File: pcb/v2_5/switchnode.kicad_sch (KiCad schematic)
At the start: 11 parts, among them Q2 IRLML6402, Q9 2SC1623 300-400

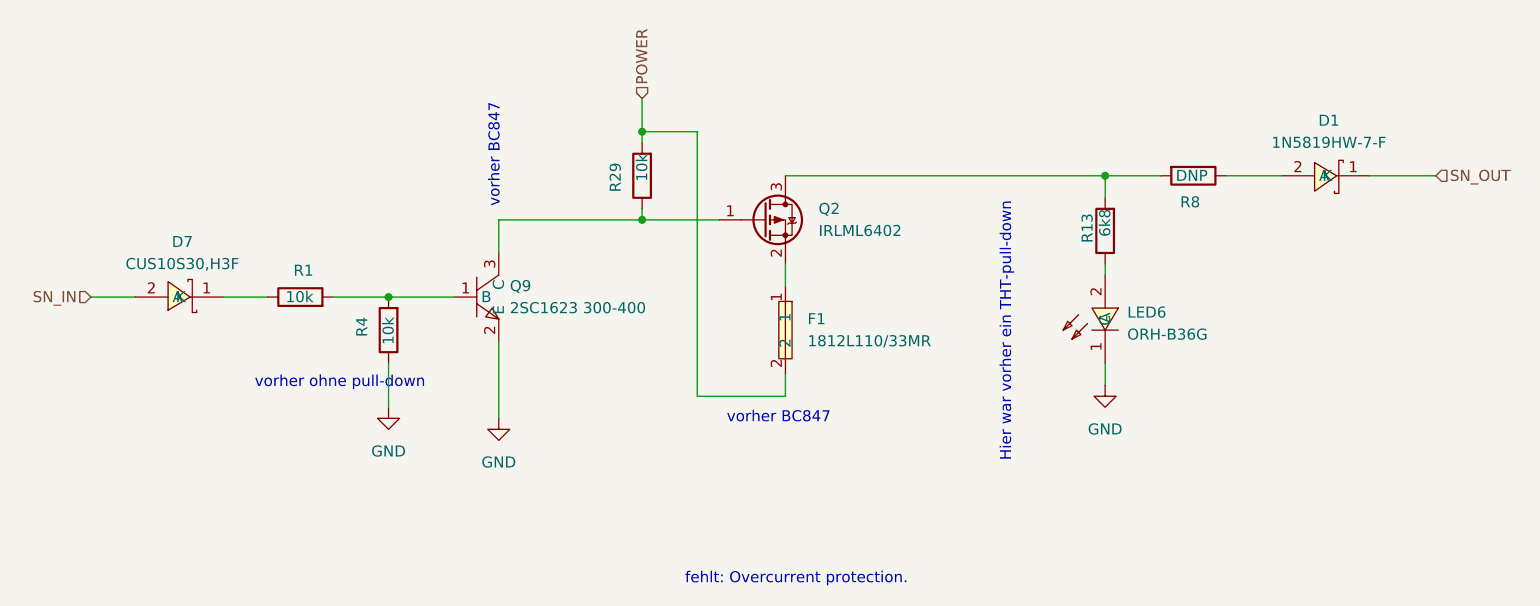
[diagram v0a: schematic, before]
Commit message: added some diodes, fuses etc
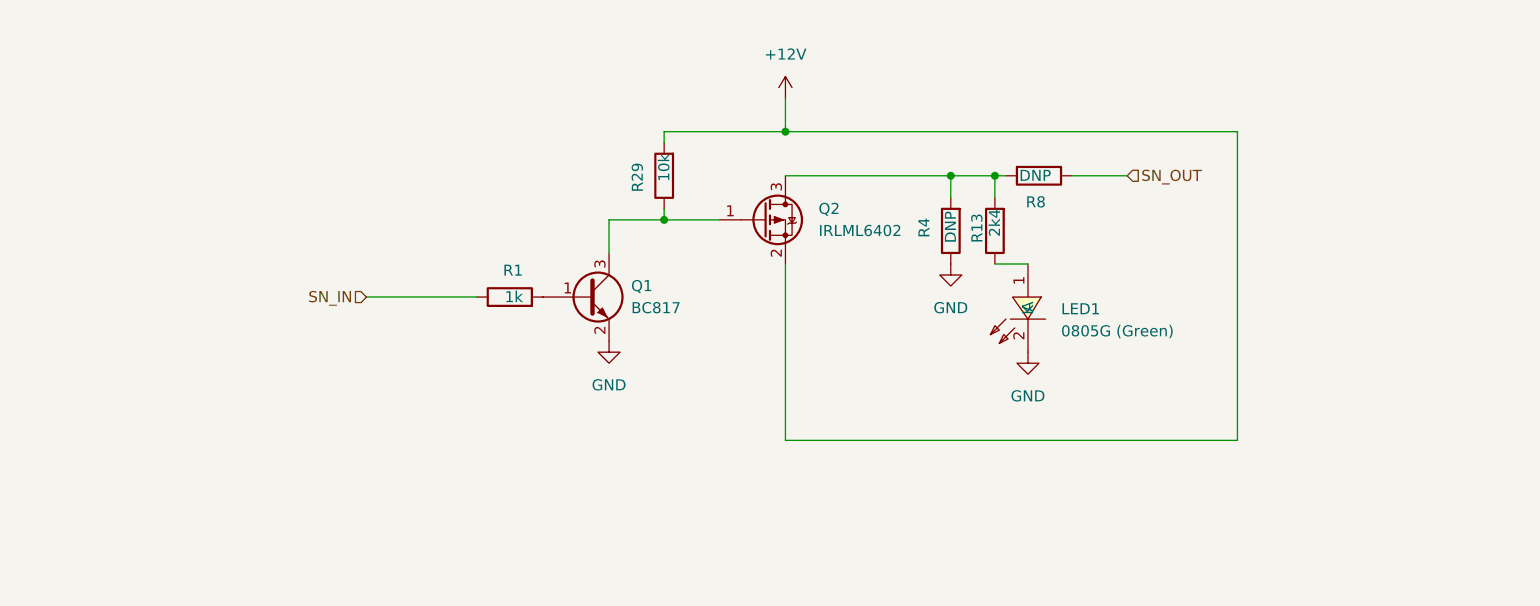
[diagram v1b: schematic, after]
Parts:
- removed D1: 1N5819HW-7-F, lcsc:SOD-123_L2.7-W1.6-LS3.7-RD, symbol lcsc:1N5819HW-7-F
- removed D7: CUS10S30,H3F, lcsc:SOD-323_L1.8-W1.3-LS2.5-RD, symbol lcsc:CUS10S30,H3F
- removed F1: 1812L110/33MR, lcsc:F1812, symbol lcsc:1812L110_33MR
- removed LED6: ORH-B36G, lcsc:LED0603-RD, symbol lcsc:ORH-B36G
- removed Q9: 2SC1623 300-400, lcsc:SOT-23-3_L2.9-W1.3-P1.90-LS2.4-BR, symbol lcsc:2SC1623300-400
- added LED1: 0805G (Green), lcsc:LED0805-R-RD, symbol lcsc:0805G(Green)
- added Q1: BC817, Package_TO_SOT_SMD:SOT-23, symbol Transistor_BJT:BC817
- R1: value 10k -> 1k
- R13: value 6k8 -> 2k4
- R4: value 10k -> DNP; footprint Resistor_SMD:R_0603_1608Metric -> Resistor_THT:R_Axial_DIN0207_L6.3mm_D2.5mm_P7.62mm_Horizontal
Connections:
- net POWER is gone; now on net +12V: R29.2
- net GND: now also LED1.2 (K), Q1.2 (E)
- net SN_IN: now also R1.1
- net SN_OUT: now also R8.1
- net at R13.1: now also LED1.1 (A)
- net at Q2.3 (D), R13.2, R8.2: now also R4.2
- net at R1.2: now also Q1.1 (B); no longer R4.2
- net at Q2.1 (G), R29.1: now also Q1.3 (C)
- net +12V: now reaches Q2.2 (S)
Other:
- note removed: "Hier war vorher ein THT-pull-down"
- note removed: "fehlt: Overcurrent protection."
- note removed: "vorher BC847"
- note removed: "vorher ohne pull-down"
- moved on the sheet: R1, R13, R29, R8
